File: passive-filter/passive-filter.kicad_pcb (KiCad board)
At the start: 2 copper layers, 100 x 100 mm, 18 parts, among them J1 AudioJack2_Switch, J2 AudioJack2_Switch, J3 Conn_01x03, J4 Conn_01x03, U1 LM318N

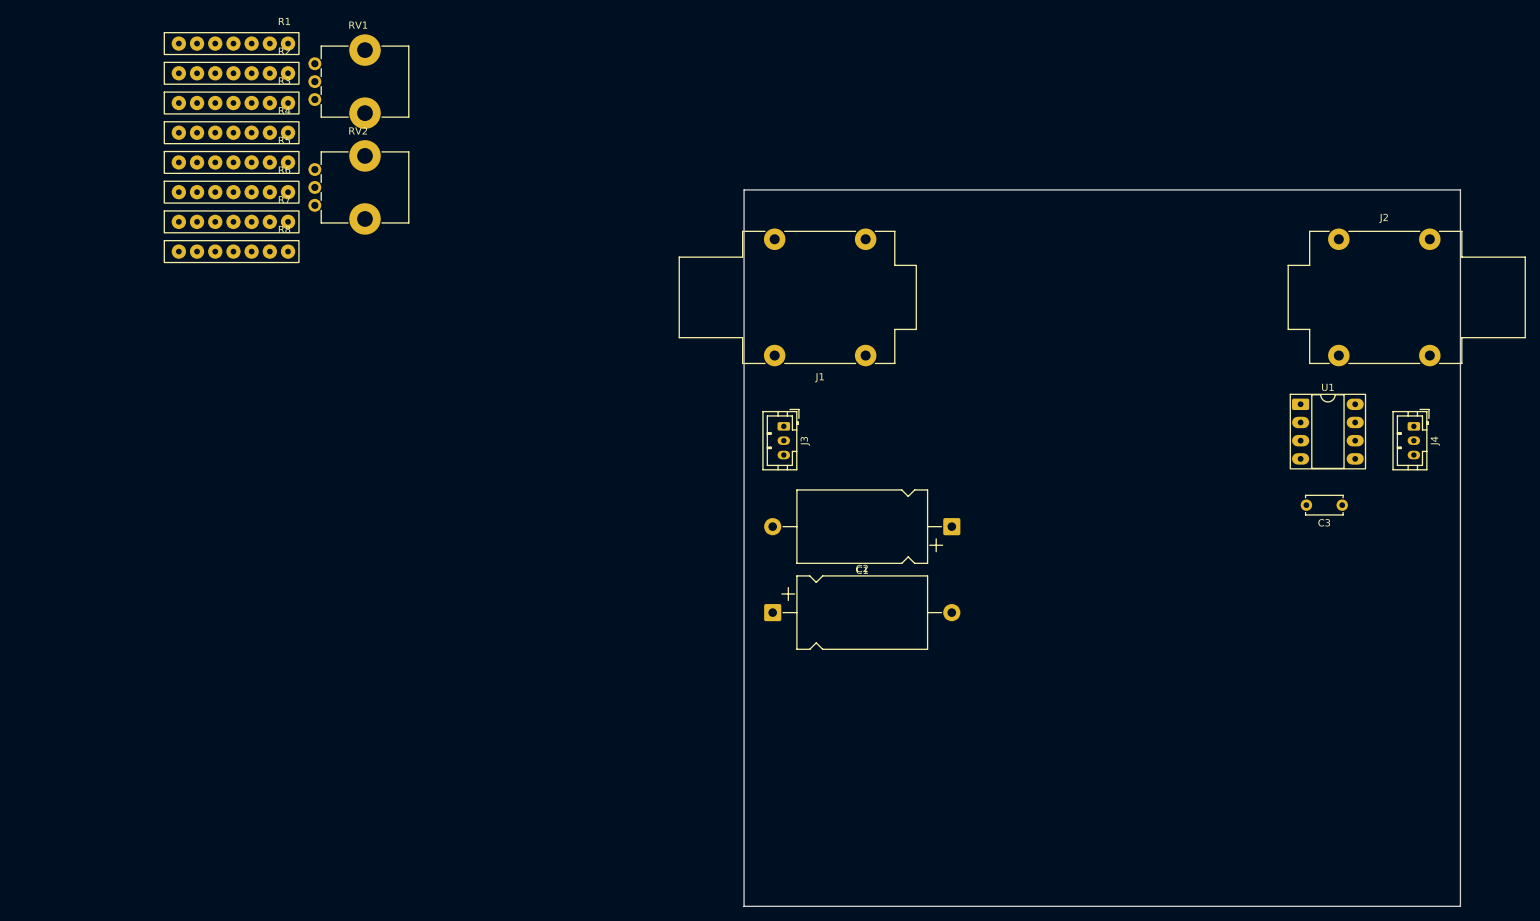
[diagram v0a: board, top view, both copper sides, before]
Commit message: passive-filter: Add PCB
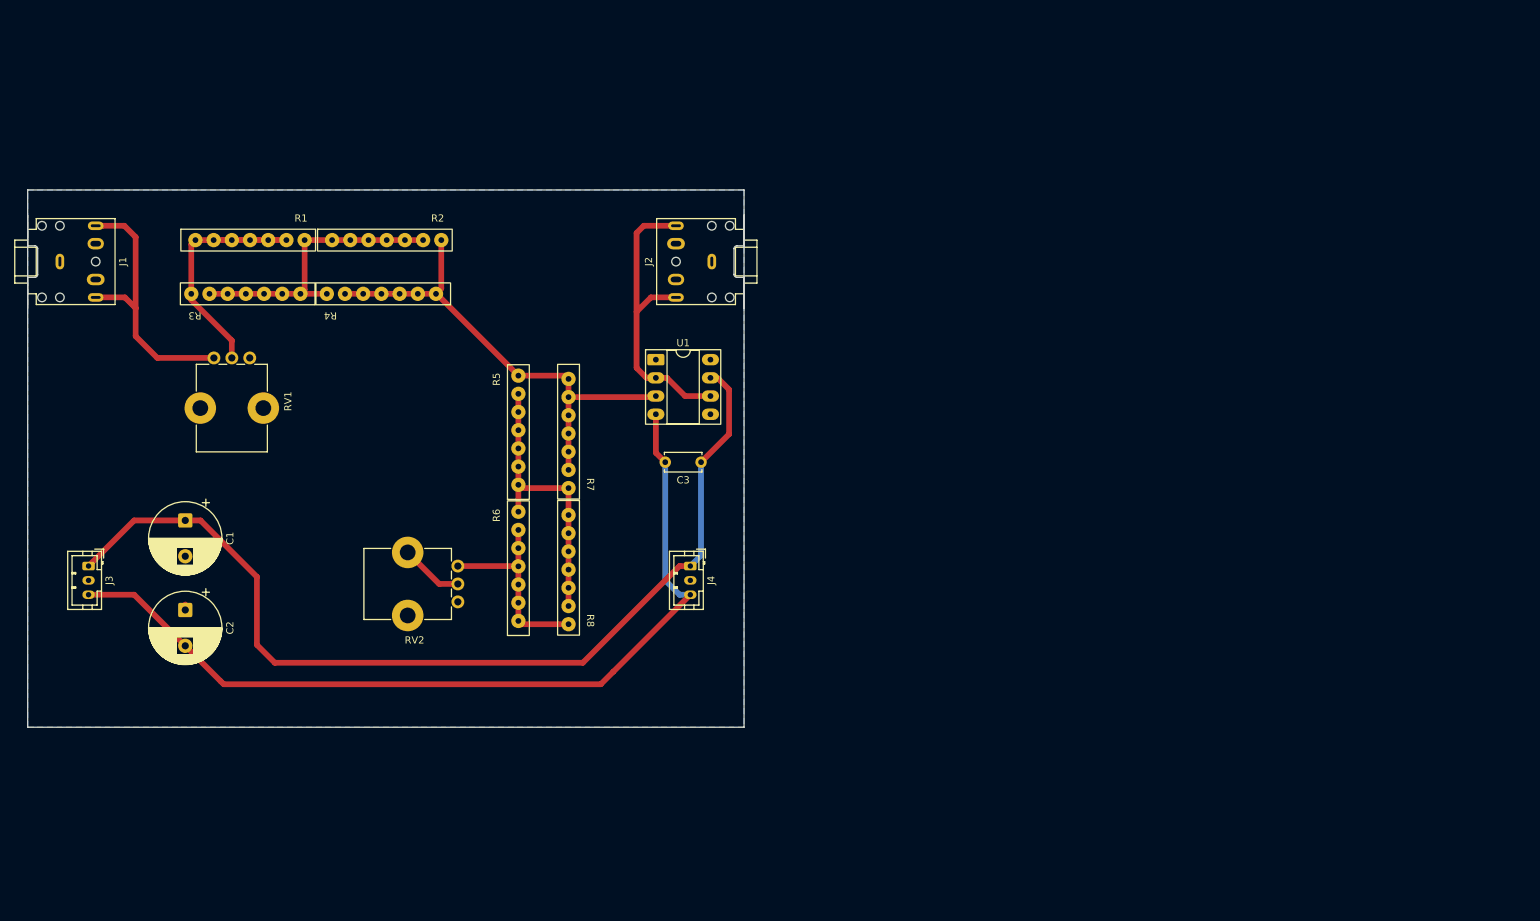
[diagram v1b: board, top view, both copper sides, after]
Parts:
- C1, C2: footprint Capacitor_THT:CP_Axial_L18.0mm_D10.0mm_P25.00mm_Horizontal -> Capacitor_THT:CP_Radial_D10.0mm_P5.00mm
- J1, J2: value AudioJack2_Switch -> AudioJack3_SwitchTR; footprint Connector_Audio:Jack_6.35mm_Neutrik_NMJ4HHD2_Horizontal -> Connector_Audio:Jack_3.5mm_CUI_SJ1-3525N_Horizontal
- RV1, RV2: value R_Potentiometer -> R_Potentiometer_MountingPin
- moved J1 113.2 mm to (54.5, 60.0), turned to -90 degrees
- moved C1 107.0 mm to (72.0, 96.1), turned to -90 degrees
- moved J4 102.9 mm to (142.5, 102.5)
- moved J3 99.0 mm to (58.5, 102.5)
- moved U1 90.2 mm to (137.7, 73.7)
- moved C3 89.7 mm to (144.0, 88.0)
- moved J2 87.6 mm to (145.5, 60.0), turned to 90 degrees
- moved C2 82.0 mm to (72.0, 108.6), turned to -90 degrees
- moved R6 66.4 mm to (118.5, 103.0), turned to 90 degrees
- moved R8 64.5 mm to (125.5, 102.5), turned to -90 degrees
- moved R7 55.5 mm to (125.5, 83.5), turned to -90 degrees
- moved R5 55.3 mm to (118.5, 84.0), turned to 90 degrees
- moved RV2 54.2 mm to (110.0, 102.5), turned to 180 degrees
- moved RV1 38.7 mm to (76.0, 73.5), turned to -90 degrees
- moved R2 31.6 mm to (99.6, 57.0)
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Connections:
- J1 pad T: Net-(J1-PadT) -> Net-(J1-PadR)
- R2 pad 1: Net-(R1-Pad2) -> Net-(U1-+)
- R2 pad 2: Net-(U1-+) -> Net-(R1-Pad1)
- R3 pad 1: Net-(R1-Pad1) -> Net-(R1-Pad2)
- R3 pad 2: Net-(R1-Pad2) -> Net-(R1-Pad1)
- R4 pad 1: Net-(R1-Pad2) -> Net-(R1-Pad1)
- R5 pad 1: Net-(R5-Pad1) -> Net-(U1-+)
- R5 pad 2: Net-(U1-+) -> Net-(R5-Pad2)
- R6 pad 1: Net-(R6-Pad1) -> Net-(R5-Pad2)
- R6 pad 2: Net-(R5-Pad1) -> Net-(R6-Pad2)
- R7 pad 1: Net-(R5-Pad1) -> Net-(R5-Pad2)
- R8 pad 1: Net-(R6-Pad1) -> Net-(R6-Pad2)
- R8 pad 2: Net-(R5-Pad1) -> Net-(R5-Pad2)
- RV1 pad 1: Net-(J1-PadT) -> Net-(J1-PadR)
- RV1 pad 2: Net-(R1-Pad1) -> Net-(R1-Pad2)
- RV1 pad MP: (no net) -> GND
- RV2 pad 1: Net-(R6-Pad1) -> Net-(R6-Pad2)
- RV2 pad MP: (no net) -> GND
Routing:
- net VDD: track 0.00 -> 136.2 mm
- net VEE: track 0.00 -> 122.4 mm
- net Net-(U1-+): track 0.00 -> 68.9 mm
- net Net-(U1--): track 0.00 -> 43.0 mm
- net Net-(R1-Pad2): track 0.00 -> 41.9 mm
- net Net-(R1-Pad1): track 0.00 -> 40.7 mm
- net Net-(R5-Pad2): track 0.00 -> 40.1 mm
- net Net-(J1-PadR): track 0.00 -> 39.4 mm
- net Net-(R6-Pad2): track 0.00 -> 28.4 mm
- net GND: track 0.00 -> 9.59 mm
- added copper zone on B.Cu, net GND
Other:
- board size 100 x 100 mm -> 100 x 75 mm

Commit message: passive-filter: Add PCB v2
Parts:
- moved RV1 16.1 mm to (80.0, 57.9), turned to 180 degrees
- moved RV2 13.6 mm to (123.0, 106.5), turned to -90 degrees
- moved C2 13.5 mm to (71.5, 95.1)
- moved C1 12.0 mm to (71.0, 108.1)
- moved R1 11.4 mm to (92.0, 57.0)
- moved R2 11.4 mm to (111.0, 57.0)
- moved R3 11.4 mm to (92.4, 64.5)
- moved R4 11.4 mm to (111.3, 64.5)
- moved R5 9.12 mm to (122.0, 75.6)
- moved R6 9.12 mm to (122.0, 94.6)
- moved R7 9.12 mm to (129.0, 75.1)
- moved R8 9.12 mm to (129.0, 94.1)
- moved C3 5.00 mm to (139.0, 88.0), turned to 0 degrees
- moved J3 4.00 mm to (58.5, 106.5), turned to 90 degrees
- moved J4 4.00 mm to (142.5, 106.5), turned to 90 degrees
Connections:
- C3 pad 1: VDD -> VEE
- C3 pad 2: VEE -> VDD
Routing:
- net Net-(U1-+): track 68.9 -> 54.5 mm
- net VEE: track 122.4 -> 136.1 mm
- net GND: track 9.59 -> 0.00 mm
- net Net-(R1-Pad2): track 41.9 -> 36.1 mm
- net Net-(J1-PadR): track 39.4 -> 34.9 mm
- net Net-(R6-Pad2): track 28.4 -> 25.1 mm
- net VDD: track 136.2 -> 139.4 mm
